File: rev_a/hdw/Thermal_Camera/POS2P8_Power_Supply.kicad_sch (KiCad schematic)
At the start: 0 parts

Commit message: added some power supplies
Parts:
- added C? (x3): 10uF, Capacitors_SMD:C_0603, symbol Custom_Library:C_Custom
- added C?: 0.1uF, Capacitors_SMD:C_0603, symbol Custom_Library:C_Custom
- added R? (x2): 10k, Resistors_SMD:R_0603, symbol Custom_Library:R_Custom
- added R?: 1.15k, Resistors_SMD:R_0603, symbol Custom_Library:R_Custom
- added R?: 2.87k, Resistors_SMD:R_0603, symbol Custom_Library:R_Custom
- added TP?: TP, Custom Footprints Library:Test_Point, symbol Custom_Library:TP
- added U?: TPS7A92, Package_DFN_QFN:Texas_S-PDSO-N10_EP1.2x2mm, symbol Custom_Library:TPS7A91
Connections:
- new net: R?.1, R?.2, U?.3 (FB)
- new net: C?.1, U?.8 (NR/SS)
- new net +2.8V: C?.1, C?.1, R?.1, TP?.1 (TP), U?.1 (OUT), U?.2 (OUT)
- new net +3.3V: C?.1, R?.1, U?.10 (IN), U?.6 (SS_CTRL), U?.9 (IN)
- new net GND: C?.2, C?.2, C?.2, C?.2, R?.2, R?.2, U?.11 (GND), U?.4 (GND)
- new net POS2P8_PGOOD: R?.2, U?.5 (PG)
- new net POS2P8_RUN: R?.1, U?.7 (EN)

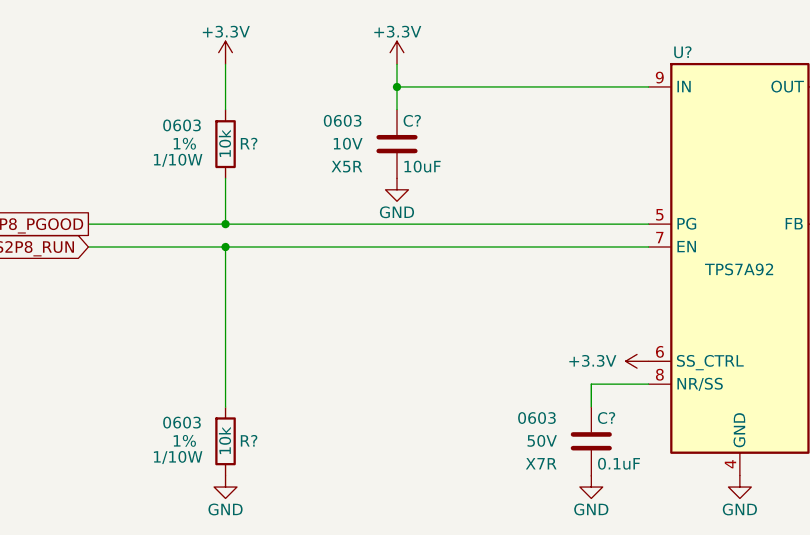
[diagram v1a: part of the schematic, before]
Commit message: changed a lot of circuits from +3.3V to +3.0V VDD
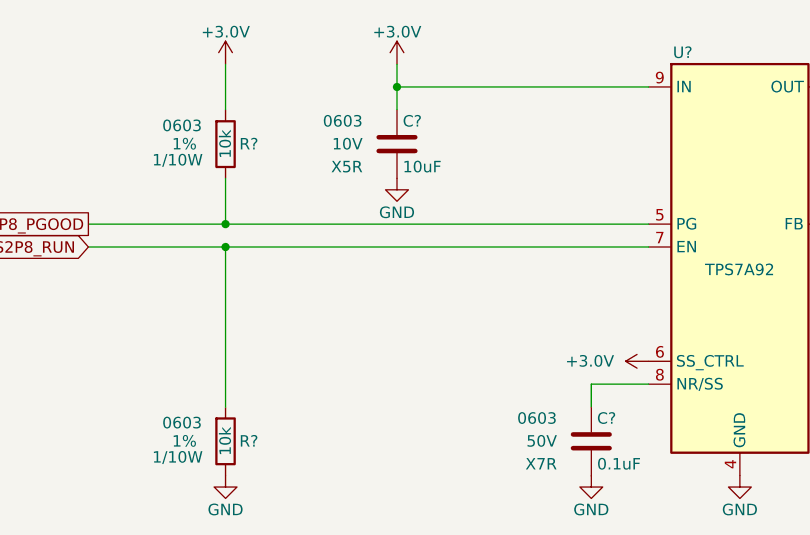
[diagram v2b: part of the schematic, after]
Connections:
- net +3.3V renamed +3.0V
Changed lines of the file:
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@@
+    )
+  )
+  (symbol (lib_id "Custom Library:+3.0V") (at 125.73 103.505 90) (unit 1)
+    (in_bom yes) (on_board yes) (dnp no)
+    (property "Reference" "#PWR0803" (at 129.54 103.505 0)
+      (effects (font (size 1.27 1.27)) hide)
+    )
+    (property "Value" "+3.0V" (at 121.92 103.505 90)
+      (effects (font (size 1.27 1.27)) (justify left))
+    )
+    (property "Footprint" "" (at 125.73 103.505 0)
+      (effects (font (size 1.27 1.27)) hide)
+    )
+    (property "Datasheet" "" (at 125.73 103.505 0)
+      (effects (font (size 1.27 1.27)) hide)
+    )
+    (pin "1")
+    (instances
+      (project "Thermal_Camera"
+        (path "/4bd21e0b-5408-4b93-866e-c82ac5b31fa9/cb0180f5-1543-4708-8311-b1b82e278e59"
+          (reference "#PWR0803") (unit 1)
+        )
+      )
     )
   )
@@
     )
   )
+  (symbol (lib_id "Custom Library:+3.0V") (at 97.79 70.485 0) (unit 1)
+    (in_bom yes) (on_board yes) (dnp no)
+    (property "Reference" "#PWR0801" (at 97.79 74.295 0)
+      (effects (font (size 1.27 1.27)) hide)
+    )
+    (property "Value" "+3.0V" (at 97.79 66.929 0)
+      (effects (font (size 1.27 1.27)))
+    )
+    (property "Footprint" "" (at 97.79 70.485 0)
+      (effects (font (size 1.27 1.27)) hide)
+    )
+    (property "Datasheet" "" (at 97.79 70.485 0)
+      (effects (font (size 1.27 1.27)) hide)
+    )
+    (pin "1")
+    (instances
+      (project "Thermal_Camera"
+        (path "/4bd21e0b-5408-4b93-866e-c82ac5b31fa9/cb0180f5-1543-4708-8311-b1b82e278e59"
+          (reference "#PWR0801") (unit 1)
+        )
+      )
+    )
+  )
   (symbol (lib_id "Custom_Library:C_Custom") (at 154.94 79.375 0) (unit 1)
     (in_bom yes) (on_board yes) (dnp no)
@@
     )
   )
-  (symbol (lib_id "power:+3.3V") (at 125.73 103.505 90) (unit 1)
-    (in_bom yes) (on_board yes) (dnp no)
-    (property "Reference" "#PWR01021" (at 129.54 103.505 0)
-      (effects (font (size 1.27 1.27)) hide)
-    )
-    (property "Value" "+3.3V" (at 122.174 103.505 90)
-      (effects (font (size 1.27 1.27)) (justify left))
-    )
-    (property "Footprint" "" (at 125.73 103.505 0)
-      (effects (font (size 1.27 1.27)) hide)
-    )
-    (property "Datasheet" "" (at 125.73 103.505 0)
-      (effects (font (size 1.27 1.27)) hide)
-    )
-    (pin "1")
-    (instances
-      (project "Thermal_Camera"
-        (path "/4bd21e0b-5408-4b93-866e-c82ac5b31fa9/cb0180f5-1543-4708-8311-b1b82e278e59"
-          (reference "#PWR01021") (unit 1)
-        )
-      )
-    )
-  )
   (symbol (lib_id "Custom_Library:TP") (at 171.45 70.485 0) (unit 1)
     (in_bom yes) (on_board yes) (dnp no)
@@
         (path "/fc908724-b650-4421-b3fb-90738df6e526/00000000-0000-0000-0000-00005e9e0ea5"
           (reference "R?") (unit 1)
-        )
-      )
-    )
-  )
-  (symbol (lib_id "power:+3.3V") (at 97.79 70.485 0) (unit 1)
-    (in_bom yes) (on_board yes) (dnp no)
-    (property "Reference" "#PWR01017" (at 97.79 74.295 0)
-      (effects (font (size 1.27 1.27)) hide)
-    )
-    (property "Value" "+3.3V" (at 97.79 66.929 0)
-      (effects (font (size 1.27 1.27)))
-    )
-    (property "Footprint" "" (at 97.79 70.485 0)
-      (effects (font (size 1.27 1.27)) hide)
-    )
-    (property "Datasheet" "" (at 97.79 70.485 0)
-      (effects (font (size 1.27 1.27)) hide)
-    )
-    (pin "1")
-    (instances
-      (project "Thermal_Camera"
-        (path "/4bd21e0b-5408-4b93-866e-c82ac5b31fa9/cb0180f5-1543-4708-8311-b1b82e278e59"
-          (reference "#PWR01017") (unit 1)
         )
       )
@@
     )
   )
+  (symbol (lib_id "Custom Library:+3.0V") (at 78.74 70.485 0) (unit 1)
+    (in_bom yes) (on_board yes) (dnp no)
+    (property "Reference" "#PWR0802" (at 78.74 74.295 0)
+      (effects (font (size 1.27 1.27)) hide)
+    )
+    (property "Value" "+3.0V" (at 78.74 66.929 0)
+      (effects (font (size 1.27 1.27)))
+    )
+    (property "Footprint" "" (at 78.74 70.485 0)
+      (effects (font (size 1.27 1.27)) hide)
+    )
+    (property "Datasheet" "" (at 78.74 70.485 0)
+      (effects (font (size 1.27 1.27)) hide)
+    )
+    (pin "1")
+    (instances
+      (project "Thermal_Camera"
+        (path "/4bd21e0b-5408-4b93-866e-c82ac5b31fa9/cb0180f5-1543-4708-8311-b1b82e278e59"
+          (reference "#PWR0802") (unit 1)
+        )
+      )
+    )
+  )
   (symbol (lib_id "power:GND") (at 154.94 83.185 0) (unit 1)
     (in_bom yes) (on_board yes) (dnp no)
@@
         )
       )
-    )
-  )
-  (symbol (lib_id "power:+3.3V") (at 78.74 70.485 0) (unit 1)
-    (in_bom yes) (on_board yes) (dnp no)
-    (property "Reference" "#PWR?" (at 78.74 74.295 0)
-      (effects (font (size 1.27 1.27)) hide)
-    )
-    (property "Value" "+3.3V" (at 78.74 66.929 0)
-      (effects (font (size 1.27 1.27)))
-    )
-    (property "Footprint" "" (at 78.74 70.485 0)
-      (effects (font (size 1.27 1.27)) hide)
-    )
-    (property "Datasheet" "" (at 78.74 70.485 0)
-      (effects (font (size 1.27 1.27)) hide)
-    )
-    (pin "1")
-    (instances
-      (project "Analog_Clock"
-        (path "/0dc9b974-a945-4291-bc55-04b8e342b0e5/00000000-0000-0000-0000-00005e939eaf"
-          (reference "#PWR?") (unit 1)
-        )
-      )
-      (project "Nixie_Clock_Core"
-        (path "/16fdce21-b570-4d81-a458-e8839d611806/0953f70f-0c64-48c1-b5cf-d1f41f95ef1f"
-          (reference "#PWR0805") (unit 1)
-        )
-      )
-      (project "Thermal_Camera"
-        (path "/4bd21e0b-5408-4b93-866e-c82ac5b31fa9/c8b41008-ee29-40ae-a4f4-13001b750237"
-          (reference "#PWR0905") (unit 1)
-        )
-        (path "/4bd21e0b-5408-4b93-866e-c82ac5b31fa9/cb0180f5-1543-4708-8311-b1b82e278e59"
-          (reference "#PWR01025") (unit 1)
-        )
-      )

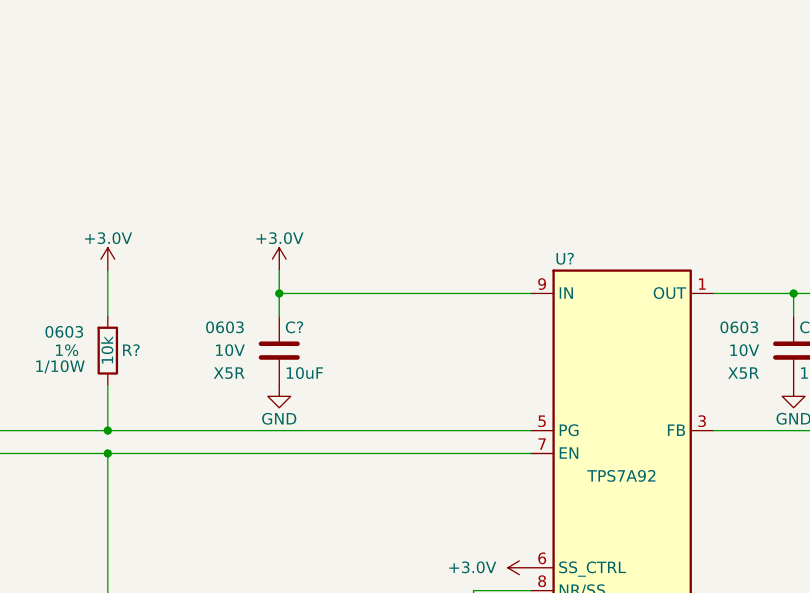
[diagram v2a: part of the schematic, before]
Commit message: added new telemetry circuits
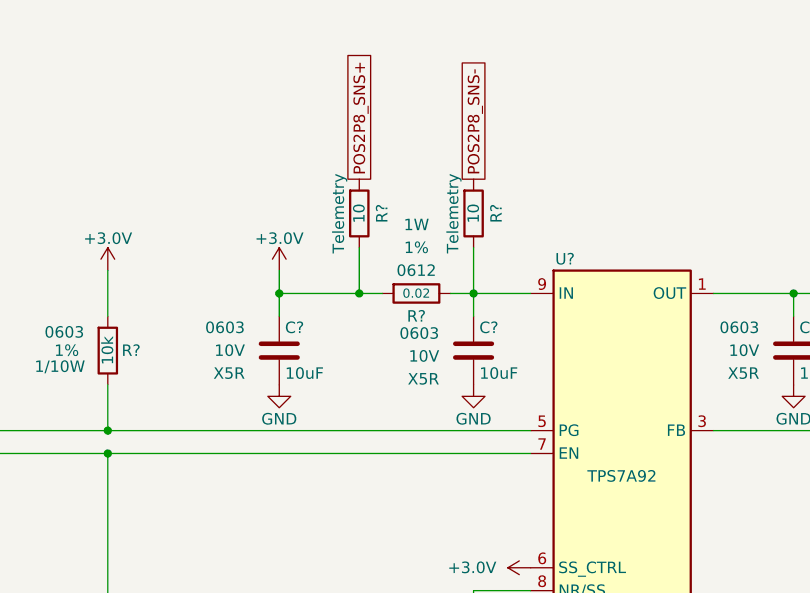
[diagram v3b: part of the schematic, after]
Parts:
- added C?: 10uF, Capacitors_SMD:C_0603, symbol Custom_Library:C_Custom
- added R? (x2): 10, Resistors_SMD:R_0603, symbol Custom_Library:R_Custom
- added R?: 0.02, Resistors_SMD:R_0612, symbol Custom_Library:R_Custom
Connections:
- net +3.0V: now also R?.1, R?.2; no longer U?.10 (IN), U?.9 (IN)
- net GND: now also C?.2
- new net: C?.1, R?.2, R?.2, U?.10 (IN), U?.9 (IN)
- new net POS2P8_SNS+: R?.1
- new net POS2P8_SNS-: R?.1

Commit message: lots of random schematic progress
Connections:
- net +3.0V: no longer U?.6 (SS_CTRL)
- net GND: now also U?.6 (SS_CTRL)
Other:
- moved on the sheet: C?, R?, TP?, U?

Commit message: lots of schematic progress
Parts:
- C801, C802, C804, C805: renamed from C?; footprint Capacitors_SMD:C_0603 -> (none); Digi-Key PN 399-8153-1-ND -> (none); display_footprint 0603 -> (none)
- C803: renamed from C?; footprint Capacitors_SMD:C_0603 -> (none); Digi-Key PN 1276-1935-1-ND -> (none); display_footprint 0603 -> (none)
- R806: renamed from R?; footprint Resistors_SMD:R_0603 -> (none); Wattage 1/10W -> (none); display_footprint 0603 -> (none)
- R807: renamed from R?; footprint Resistors_SMD:R_0603 -> (none); Digi-Key PN 541-1.15KHCT-ND -> (none); Wattage 1/10W -> (none); display_footprint 0603 -> (none)
- R? (x2): footprint Resistors_SMD:R_0603 -> (none); Digi-Key PN 541-10.0KHCT-ND -> (none); Wattage 1/10W -> (none); display_footprint 0603 -> (none)
- R? (x2): footprint Resistors_SMD:R_0603 -> (none); Digi-Key PN 541-10.0HCT-ND -> (none); Wattage 1/10W -> (none); display_footprint 0603 -> (none)
- gave numbers to parts that had none: 2

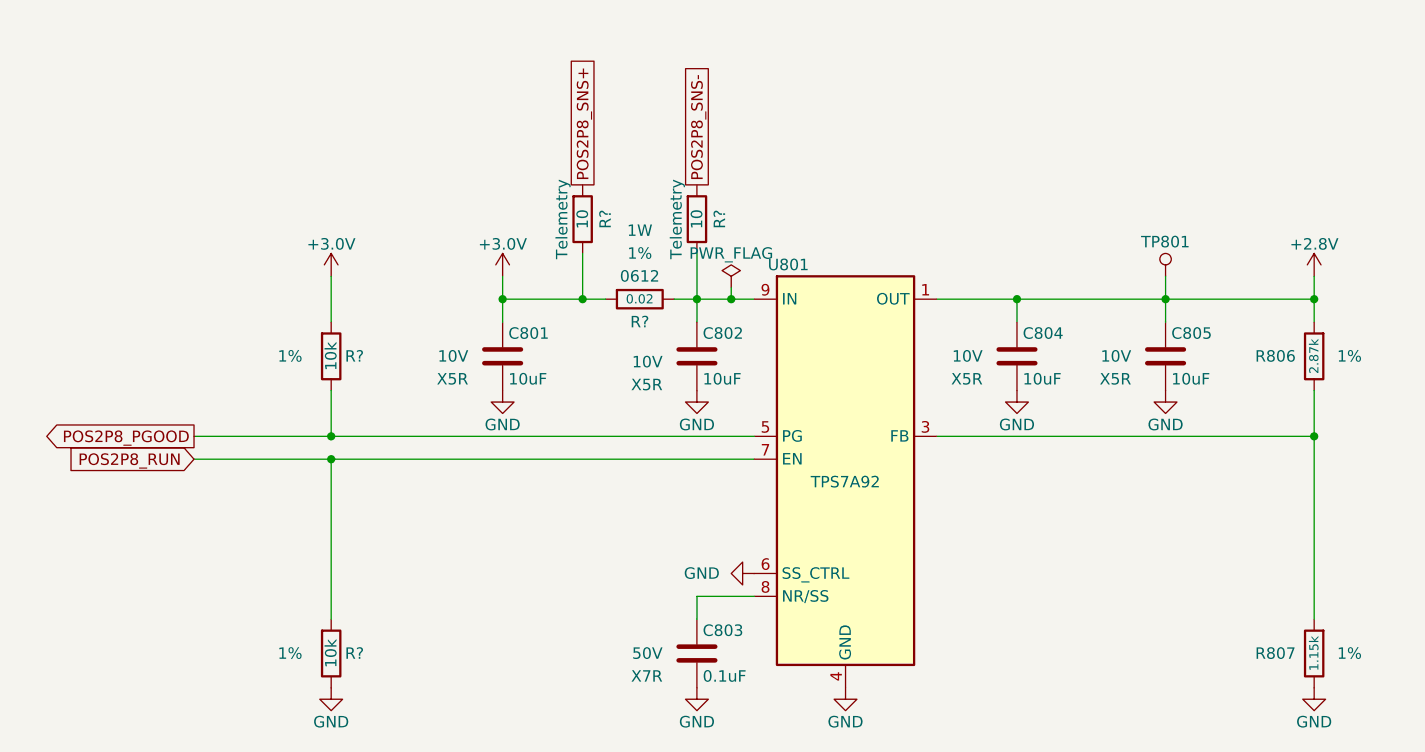
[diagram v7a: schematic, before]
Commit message: assigned a ton of footprints
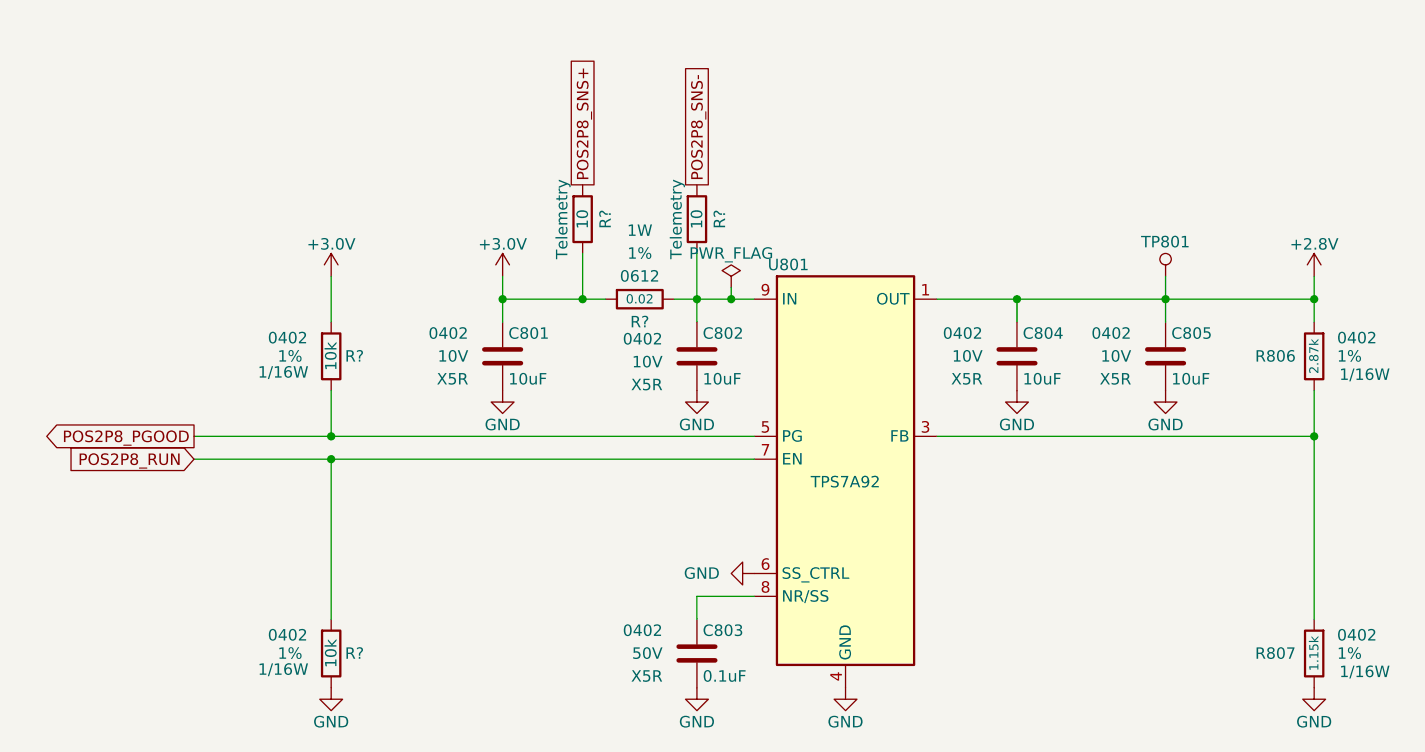
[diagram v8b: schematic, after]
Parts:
- C801, C802, C804, C805: footprint (none) -> Capacitors_SMD:C_0402; display_footprint (none) -> 0402
- C803: footprint (none) -> Capacitors_SMD:C_0402; Dielectric X7R -> X5R; display_footprint (none) -> 0402
- R806, R807, R? (x4): footprint (none) -> Resistors_SMD:R_0402; Wattage (none) -> 1/16W; display_footprint (none) -> 0402
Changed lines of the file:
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@@
 			)
 		)
-		(property "Footprint" ""
+		(property "Footprint" "Capacitors_SMD:C_0402"
 			(at 155.9052 83.82 0)
 			(effects
@@
 			)
 		)
-		(property "display_footprint" ""
+		(property "display_footprint" "0402"
 			(at 151.13 77.47 0)
 			(effects
@@
 			)
 		)
-		(property "Footprint" ""
+		(property "Footprint" "Resistors_SMD:R_0402"
 			(at 78.74 80.01 0)
 			(effects
@@
 			)
 		)
-		(property "display_footprint" ""
+		(property "display_footprint" "0402"
 			(at 73.914 77.978 0)
 			(effects
@@
 			)
 		)
-		(property "Wattage" ""
+		(property "Wattage" "1/16W"
 			(at 73.406 81.788 0)
 			(effects
@@
 			)
 		)
-		(property "Footprint" ""
+		(property "Footprint" "Resistors_SMD:R_0402"
 			(at 106.68 64.77 0)
 			(effects
@@
 			)
 		)
-		(property "display_footprint" ""
+		(property "display_footprint" "0402"
 			(at 104.14 64.77 90)
 			(effects
@@
 			)
 		)
-		(property "Wattage" ""
+		(property "Wattage" "1/16W"
 			(at 99.06 64.77 90)
 			(effects
@@
 			)
 		)
-		(property "Footprint" ""
+		(property "Footprint" "Resistors_SMD:R_0402"
 			(at 187.96 113.03 0)
 			(effects
@@
 			)
 		)
-		(property "display_footprint" ""
+		(property "display_footprint" "0402"
 			(at 190.5 110.998 0)
 			(effects
@@
 			)
 		)
-		(property "Wattage" ""
+		(property "Wattage" "1/16W"
 			(at 190.754 115.062 0)
 			(effects
@@
 			)
 		)
-		(property "Footprint" ""
+		(property "Footprint" "Capacitors_SMD:C_0402"
 			(at 172.4152 83.82 0)
 			(effects
@@
 			)
 		)
-		(property "display_footprint" ""
+		(property "display_footprint" "0402"
 			(at 167.64 77.47 0)
 			(effects
@@
 			)
 		)
-		(property "Footprint" ""
+		(property "Footprint" "Resistors_SMD:R_0402"
 			(at 119.38 64.77 0)
 			(effects
@@
 			)
 		)
-		(property "display_footprint" ""
+		(property "display_footprint" "0402"
 			(at 116.84 64.77 90)
 			(effects
@@
 			)
 		)
-		(property "Wattage" ""
+		(property "Wattage" "1/16W"
 			(at 111.76 64.77 90)
 			(effects
@@
 			)
 		)
-		(property "Footprint" ""
+		(property "Footprint" "Capacitors_SMD:C_0402"
 			(at 120.3452 83.82 0)
 			(effects
@@
 			)
 		)
-		(property "display_footprint" ""
+		(property "display_footprint" "0402"
 			(at 115.57 78.105 0)
 			(effects
@@
 			)
 		)
-		(property "Footprint" ""
+		(property "Footprint" "Resistors_SMD:R_0402"
 			(at 187.96 80.01 0)
 			(effects
@@
 			)
 		)
-		(property "display_footprint" ""
+		(property "display_footprint" "0402"
 			(at 190.5 77.978 0)
 			(effects
@@
 			)
 		)
-		(property "Wattage" ""
+		(property "Wattage" "1/16W"
 			(at 190.754 82.042 0)
 			(effects
@@
 			)
 		)
-		(property "Footprint" ""
+		(property "Footprint" "Capacitors_SMD:C_0402"
 			(at 120.3452 116.84 0)
 			(effects
@@
 			)
 		)
-		(property "display_footprint" ""
+		(property "display_footprint" "0402"
 			(at 115.57 110.49 0)
 			(effects
@@
 			)
 		)
-		(property "Dielectric" "X7R"
+		(property "Dielectric" "X5R"
 			(at 115.57 115.57 0)
 			(effects
@@
 			)
 		)
-		(property "Footprint" ""
+		(property "Footprint" "Resistors_SMD:R_0402"
 			(at 78.74 113.03 0)
 			(effects
@@
 			)
 		)
-		(property "display_footprint" ""
+		(property "display_footprint" "0402"
 			(at 73.914 110.998 0)
 			(effects
@@
 			)
 		)
-		(property "Wattage" ""
+		(property "Wattage" "1/16W"
 			(at 73.406 114.808 0)
 			(effects
@@
 			)
 		)
-		(property "Footprint" ""
+		(property "Footprint" "Capacitors_SMD:C_0402"
 			(at 98.7552 83.82 0)
 			(effects
@@
 			)
 		)
-		(property "display_footprint" ""
+		(property "display_footprint" "0402"
 			(at 93.98 77.47 0)
 			(effects
